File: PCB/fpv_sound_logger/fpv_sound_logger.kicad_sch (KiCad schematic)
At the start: 47 parts, among them CN1 SM04B-SRSS-TB(LF)(SN), IC1 W25Q128JVSIQ, IC2 NCP1117ST33T3G, J1 DM3D-SF, U1 RP2040, U2 INMP441ACEZ-R7, Y1 ABM8-272-T3

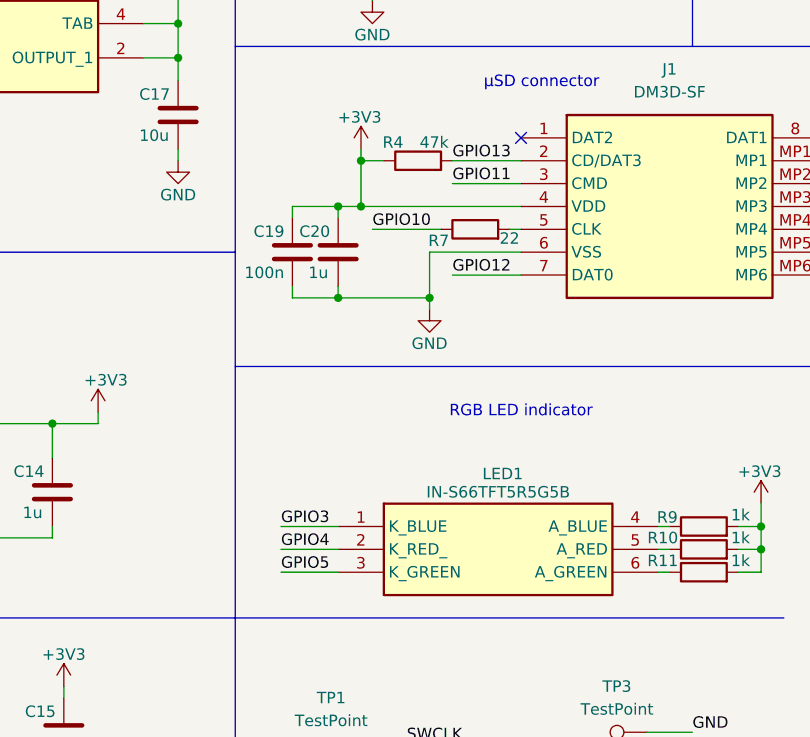
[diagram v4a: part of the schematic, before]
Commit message: PCB: finised routing - Changed clearance from 0.2 to 0.15 in the net class settings. - Increased track width from 0.3 to 0.4 for improved signal integrity. - Added a new net class for POWER with pattern GND. - Adjusted positions of GPIO labels for better alignment in the schematic:   - Moved GPIO3 from (119.38, 160.02) to (119.38, 165.1).   - Moved GPIO5 from (119.38, 165.1) to (119.38, 160.02).   - Moved GPIO10 from (129.54, 127) to (138.43, 121.92).   - Moved GPIO11 from (138.43, 121.92) to (129.54, 127).
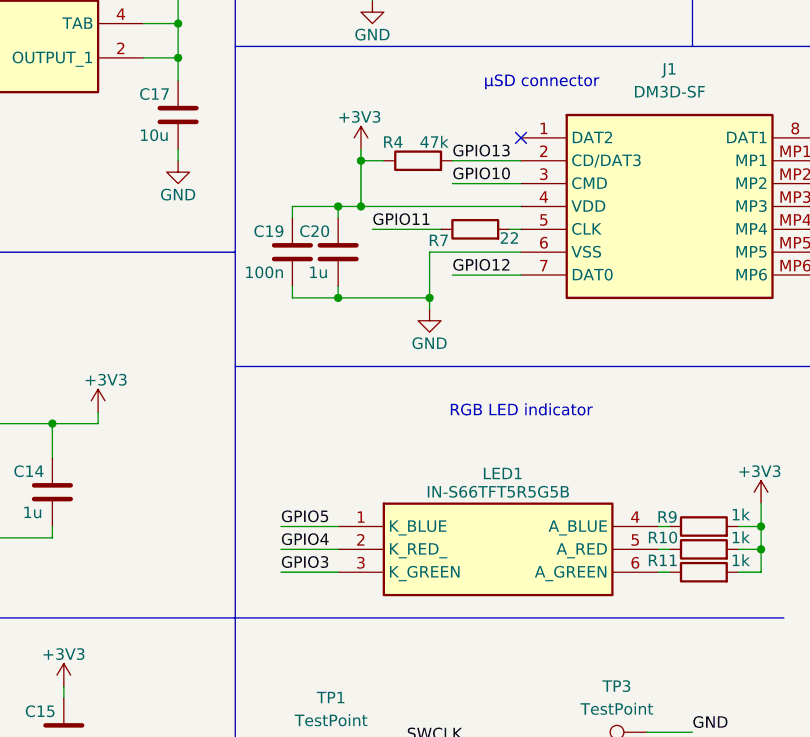
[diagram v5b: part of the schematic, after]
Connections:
- net GPIO10: now also J1.3 (CMD); no longer R7.1
- net GPIO11: now also R7.1; no longer J1.3 (CMD)
- net GPIO3: now also LED1.3 (K_GREEN); no longer LED1.1 (K_BLUE)
- net GPIO5: now also LED1.1 (K_BLUE); no longer LED1.3 (K_GREEN)
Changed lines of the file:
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@@
 	)
 	(label "GPIO3"
-		(at 119.38 160.02 0)
+		(at 119.38 165.1 0)
 		(effects
 			(font
@@
 	)
 	(label "GPIO5"
-		(at 119.38 165.1 0)
+		(at 119.38 160.02 0)
 		(effects
 			(font
@@
 	)
 	(label "GPIO10"
-		(at 129.54 127 0)
+		(at 138.43 121.92 0)
 		(effects
 			(font
@@
 	)
 	(label "GPIO11"
-		(at 138.43 121.92 0)
-		(effects
-			(font
+		(at 129.54 127 0)
+		(effects
+			(font

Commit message: Refactor code structure and remove redundant sections for improved readability and maintainability
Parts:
- removed C1, C10, C11, C18, C19, C2, C3, C4, C5, C6, C7: 100n, Capacitor_SMD:C_0402_1005Metric, symbol Device:C
- removed C12, C13, C14, C20, C8, C9: 1u, Capacitor_SMD:C_0402_1005Metric, symbol Device:C
- removed C15, C16, C17: 10u, Capacitor_SMD:C_0402_1005Metric, symbol Device:C
- removed CN1: SM04B-SRSS-TB(LF)(SN), fpv_sound_logger:CONN-SMD_4P-P1.00_SM04B-SRSS-TB-LF-SN, symbol SoundLogger:SM04B-SRSS-TB (LF)(SN)
- removed D1, D2: SS14, fpv_sound_logger:DIOM5227X270N, symbol SoundLogger:SS14
- removed IC1: W25Q128JVSIQ, fpv_sound_logger:SOIC127P790X216-8N, symbol SoundLogger:W25Q128JVSIQ
- removed IC2: NCP1117ST33T3G, fpv_sound_logger:SOT230P700X180-4N, symbol SoundLogger:NCP1117ST33T3G
- removed J1: DM3D-SF, fpv_sound_logger:DM3DSF, symbol SoundLogger:DM3D-SF
- removed LED1: IN-S66TFT5R5G5B, fpv_sound_logger:INS66TFT5R5G5B, symbol SoundLogger:IN-S66TFT5R5G5B
- removed R1, R2, R3: 27, Resistor_SMD:R_0402_1005Metric, symbol Device:R
- removed R10, R11, R9: 1k, Resistor_SMD:R_0402_1005Metric, symbol Device:R
- removed R4: 47k, Resistor_SMD:R_0402_1005Metric, symbol Device:R
- removed R5, R6: 5k1, Resistor_SMD:R_0402_1005Metric, symbol Device:R
- removed R7: 22, Resistor_SMD:R_0402_1005Metric, symbol Device:R
- removed R8: 10k, Resistor_SMD:R_0402_1005Metric, symbol Device:R
- removed S1: B3U-1000P, fpv_sound_logger:B3U-1000P, symbol SoundLogger:B3U-1000P
- removed TP1, TP2, TP3, TP4: TestPoint, TestPoint:TestPoint_Pad_D1.0mm, symbol Connector:TestPoint
- removed U1: RP2040, Package_DFN_QFN:QFN-56-1EP_7x7mm_P0.4mm_EP3.2x3.2mm, symbol MCU_RaspberryPi:RP2040
- removed U2: INMP441ACEZ-R7, fpv_sound_logger:MID-SMD_L4.7-W3.8_INMP441ACEZ, symbol SoundLogger:INMP441ACEZ-R7
- removed USB1: TYPE-C 16PIN 2MD(073), fpv_sound_logger:USB-C-SMD_TYPE-C-6PIN-2MD-073, symbol SoundLogger:TYPE-C 16PIN 2MD(073)
- removed Y1: ABM8-272-T3, fpv_sound_logger:ABM8272T3, symbol SoundLogger:ABM8-272-T3
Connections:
- no-connect marks 21 -> 0
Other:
- added sheet MCU (mcu.kicad_sch)
- added sheet connector (connector.kicad_sch)
- added sheet sensor (sensor.kicad_sch)
- note removed: "BOOTSEL"
- note removed: "C8 must be physically close pin 43 VREG_IN"
- note removed: "C9 must be physically close pin 45 VREG_VOUT"
- note removed: "External oscillator 12MHz"
- note removed: "Flash memory"
- note removed: "JST 4-PIN connector"
- note removed: "Microphone"
- note removed: "R1&R2 must be close to RP2040"
- note removed: "RGB LED indicator"
- note removed: "USB-C and voltage regulation"
- note removed: "µSD connector"
